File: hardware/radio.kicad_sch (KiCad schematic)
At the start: 61 parts, among them J1 105450-0101, J2 Conn_01x02, J3 Conn_01x02, J4 Conn_01x04, J5 Conn_01x02_Male, Q1 Q_PMOS_DGS, Q2 Q_NMOS_DGS, Q3 Q_NMOS_DGS, Q4 Q_PMOS_DGS, SW1 SW_BOOT, SW2 SW_RST, SW3 SW_1, SW4 Rot_Enc, SW5 SW_2, SW6 SW_3, U1 TP4056, U2 ESP32-WROOM-32, U3 TPS5432, U4 MAX98357

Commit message: routing
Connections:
- net BTN_1: now also U2.28 (IO17)
- net BTN_2: now also U2.27 (IO16)
- net BTN_3: now also U2.26 (IO4)
- net ENC_A: now also U2.5 (SENSOR_VN)
- net ENC_B: now also U2.4 (SENSOR_VP)
- net OLED_RST: now reaches U2.10 (IO25)
- net OLED_RST: now also DISP1.1 (RES)
- net CHRG: now reaches U2.29 (IO5)
- net CHRG: now also U1.7 (~{CHRG})
- net STBY: now reaches U2.30 (IO18)
- net STBY: now also U1.6 (~{STBY})
- net OLED_MOSI: now reaches U2.6 (IO34)
- net OLED_MOSI: now also DISP1.5 (DIN)
- net OLED_CLK: now reaches U2.7 (IO35)
- net OLED_CLK: now also DISP1.4 (CLK)
- net OLED_CS: now reaches U2.8 (IO32)
- net OLED_CS: now also DISP1.3 (CS)
- net OLED_DC: now reaches U2.9 (IO33)
- net OLED_DC: now also DISP1.2 (D/C)
- no-connect marks 6 -> 26
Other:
- note removed: "TODO: * CONNECT DISPLAY AND DAC/AMP TO ESP32 * CONNECT BUTTONS, ROTARY ENCODER"

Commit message: routing
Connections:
- net BTN_1: now also U2.29 (IO5); no longer U2.28 (IO17)
- net BTN_2: now also U2.26 (IO4); no longer U2.27 (IO16)
- net BTN_3: now also U2.27 (IO16); no longer U2.26 (IO4)
- net CHRG: now also U2.30 (IO18); no longer U2.29 (IO5)
- net PWR_CTRL: now also U2.28 (IO17)
- net STBY: now also U2.31 (IO19); no longer U2.30 (IO18)
- no-connect marks 26 -> 25
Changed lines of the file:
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@@
   (no_connect (at 162.56 125.73))
   (no_connect (at 162.56 130.81))
-  (no_connect (at 162.56 123.19))
   (no_connect (at 25.4 93.98))
   (no_connect (at 25.4 83.82))
@@
     (stroke (width 0) (type default) (color 0 0 0 0))
   )
+  (wire (pts (xy 162.56 123.19) (xy 167.64 123.19))
+    (stroke (width 0) (type default) (color 0 0 0 0))
+  )
   (wire (pts (xy 115.57 154.94) (xy 115.57 153.67))
     (stroke (width 0) (type default) (color 0 0 0 0))
@@
     (effects (font (size 1.27 1.27)) (justify left bottom))
   )
-  (global_label "BTN_1" (shape input) (at 167.64 118.11 0) (fields_autoplaced)
-    (effects (font (size 1.27 1.27)) (justify left))
-    (property "Intersheet References" "${INTERSHEET_REFS}" (id 0) (at 175.7983 118.0306 0)
-      (effects (font (size 1.27 1.27)) (justify left) hide)
-    )
-  )
   (global_label "OLED_CLK" (shape input) (at 248.92 95.25 180) (fields_autoplaced)
     (effects (font (size 1.27 1.27)) (justify right))
@@
     )
   )
-  (global_label "BTN_2" (shape input) (at 167.64 115.57 0) (fields_autoplaced)
+  (global_label "BTN_3" (shape input) (at 167.64 115.57 0) (fields_autoplaced)
     (effects (font (size 1.27 1.27)) (justify left))
     (property "Intersheet References" "${INTERSHEET_REFS}" (id 0) (at 175.7983 115.4906 0)
@@
     )
   )
+  (global_label "BTN_1" (shape input) (at 167.64 102.87 0) (fields_autoplaced)
+    (effects (font (size 1.27 1.27)) (justify left))
+    (property "Intersheet References" "${INTERSHEET_REFS}" (id 0) (at 175.7983 102.7906 0)
+      (effects (font (size 1.27 1.27)) (justify left) hide)
+    )
+  )
   (global_label "I2S_SD_MODE" (shape input) (at 199.39 143.51 180) (fields_autoplaced)
     (effects (font (size 1.27 1.27)) (justify right))
@@
     )
   )
-  (global_label "STBY" (shape input) (at 167.64 120.65 0) (fields_autoplaced)
-    (effects (font (size 1.27 1.27)) (justify left))
-    (property "Intersheet References" "${INTERSHEET_REFS}" (id 0) (at 174.5888 120.5706 0)
+  (global_label "PWR_CTRL" (shape input) (at 167.64 118.11 0) (fields_autoplaced)
+    (effects (font (size 1.27 1.27)) (justify left))
+    (property "Intersheet References" "${INTERSHEET_REFS}" (id 0) (at 179.5479 118.0306 0)
       (effects (font (size 1.27 1.27)) (justify left) hide)
     )
@@
     )
   )
+  (global_label "BTN_2" (shape input) (at 167.64 100.33 0) (fields_autoplaced)
+    (effects (font (size 1.27 1.27)) (justify left))
+    (property "Intersheet References" "${INTERSHEET_REFS}" (id 0) (at 175.7983 100.2506 0)
+      (effects (font (size 1.27 1.27)) (justify left) hide)
+    )
+  )
+  (global_label "CHRG" (shape input) (at 167.64 120.65 0) (fields_autoplaced)
+    (effects (font (size 1.27 1.27)) (justify left))
+    (property "Intersheet References" "${INTERSHEET_REFS}" (id 0) (at 175.1936 120.5706 0)
+      (effects (font (size 1.27 1.27)) (justify left) hide)
+    )
+  )
   (global_label "ENC_A" (shape input) (at 129.54 104.14 270) (fields_autoplaced)
     (effects (font (size 1.27 1.27)) (justify right))
@@
     )
   )
-  (global_label "BTN_3" (shape input) (at 167.64 100.33 0) (fields_autoplaced)
-    (effects (font (size 1.27 1.27)) (justify left))
-    (property "Intersheet References" "${INTERSHEET_REFS}" (id 0) (at 175.7983 100.2506 0)
-      (effects (font (size 1.27 1.27)) (justify left) hide)
-    )
-  )
   (global_label "I2S_BCLK" (shape input) (at 167.64 110.49 0) (fields_autoplaced)
     (effects (font (size 1.27 1.27)) (justify left))
@@
     )
   )
-  (global_label "CHRG" (shape input) (at 167.64 102.87 0) (fields_autoplaced)
-    (effects (font (size 1.27 1.27)) (justify left))
-    (property "Intersheet References" "${INTERSHEET_REFS}" (id 0) (at 175.1936 102.7906 0)
-      (effects (font (size 1.27 1.27)) (justify left) hide)
-    )
-  )
   (global_label "ENC_S1" (shape input) (at 107.95 116.84 0) (fields_autoplaced)
     (effects (font (size 1.27 1.27)) (justify left))
@@
       (effects (font (size 1.27 1.27)) (justify left) hide)
     )
+  )
+  (global_label "STBY" (shape input) (at 167.64 123.19 0) (fields_autoplaced)
+    (effects (font (size 1.27 1.27)) (justify left))
+    (property "Intersheet References" "${INTERSHEET_REFS}" (id 0) (at 174.5888 123.1106 0)
+      (effects (font (size 1.27 1.27)) (justify left) hide)
+    )

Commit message: fixed DRC  violations, added silkscreen legend
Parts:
- J1: sklep (none) -> https://kamami.pl/zlacza-usb/1178195-1054500101-zlacze-usb-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
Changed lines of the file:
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@@
       (effects (font (size 1.27 1.27)) (justify left bottom) hide)
+    )
+    (property "sklep" "https://kamami.pl/zlacza-usb/1178195-1054500101-zlacze-usb-typu-c-katowe.html" (id 8) (at 43.18 91.44 0)
+      (effects (font (size 1.27 1.27)) hide)
     )
     (pin "A1")

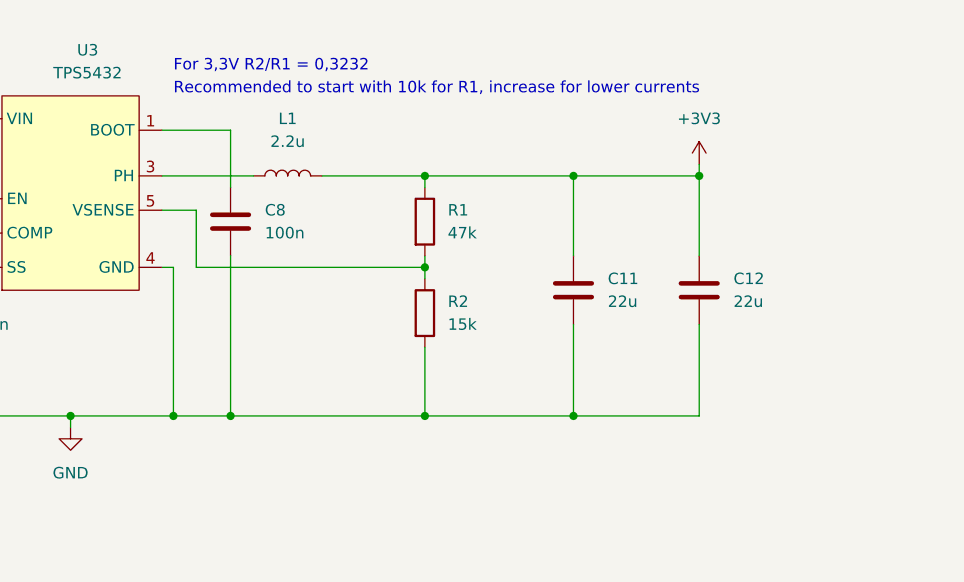
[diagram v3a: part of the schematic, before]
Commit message: Fixed C8 connection from BOOT-GND to BOOT-PH
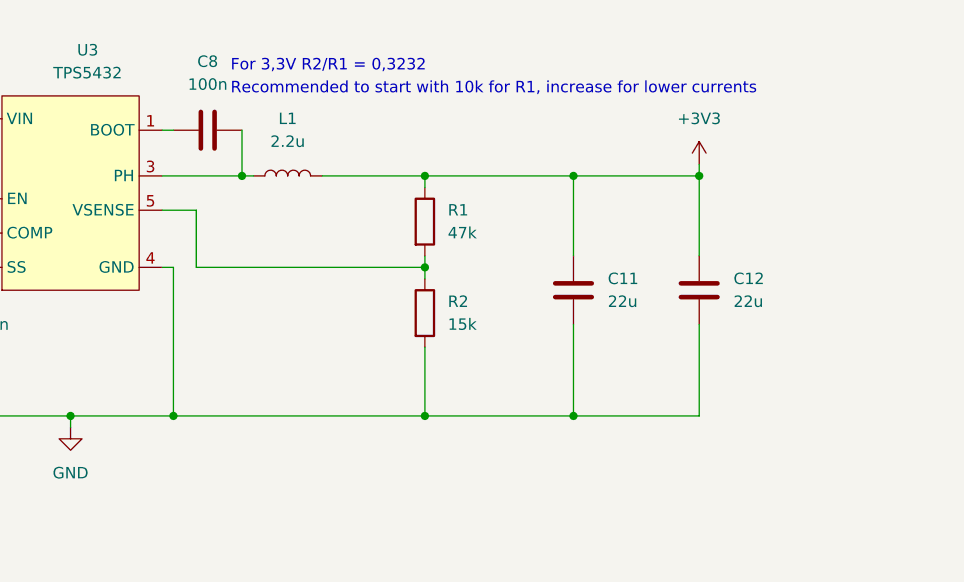
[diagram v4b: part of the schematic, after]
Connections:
- net GND: no longer C8.1
- net at L1.1, U3.3 (PH): now also C8.1
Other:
- moved on the sheet: C8
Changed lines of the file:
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@@
   (junction (at 130.81 22.86) (diameter 0) (color 0 0 0 0)
   )
-  (junction (at 222.25 55.88) (diameter 0) (color 0 0 0 0)
-  )
   (junction (at 85.09 116.84) (diameter 0) (color 0 0 0 0)
+  )
+  (junction (at 223.52 29.21) (diameter 0) (color 0 0 0 0)
   )
   (junction (at 234.95 135.89) (diameter 0) (color 0 0 0 0)
@@
     (stroke (width 0) (type default) (color 0 0 0 0))
   )
+  (wire (pts (xy 214.63 24.13) (xy 215.9 24.13))
+    (stroke (width 0) (type default) (color 0 0 0 0))
+  )
   (wire (pts (xy 19.05 39.37) (xy 19.05 43.18))
     (stroke (width 0) (type default) (color 0 0 0 0))
@@
     (stroke (width 0) (type default) (color 0 0 0 0))
   )
-  (wire (pts (xy 214.63 29.21) (xy 224.79 29.21))
+  (wire (pts (xy 214.63 29.21) (xy 223.52 29.21))
     (stroke (width 0) (type default) (color 0 0 0 0))
   )
@@
     (stroke (width 0) (type default) (color 0 0 0 0))
   )
-  (wire (pts (xy 214.63 24.13) (xy 222.25 24.13))
-    (stroke (width 0) (type default) (color 0 0 0 0))
-  )
   (wire (pts (xy 102.87 119.38) (xy 102.87 116.84))
     (stroke (width 0) (type default) (color 0 0 0 0))
@@
     (stroke (width 0) (type default) (color 0 0 0 0))
   )
+  (wire (pts (xy 223.52 24.13) (xy 223.52 29.21))
+    (stroke (width 0) (type default) (color 0 0 0 0))
+  )
   (wire (pts (xy 62.23 68.58) (xy 43.18 68.58))
     (stroke (width 0) (type default) (color 0 0 0 0))
@@
     (stroke (width 0) (type default) (color 0 0 0 0))
   )
-  (wire (pts (xy 243.84 55.88) (xy 222.25 55.88))
+  (wire (pts (xy 215.9 55.88) (xy 243.84 55.88))
     (stroke (width 0) (type default) (color 0 0 0 0))
   )
@@
     (stroke (width 0) (type default) (color 0 0 0 0))
   )
-  (wire (pts (xy 222.25 55.88) (xy 215.9 55.88))
-    (stroke (width 0) (type default) (color 0 0 0 0))
-  )
   (wire (pts (xy 85.09 115.57) (xy 85.09 116.84))
     (stroke (width 0) (type default) (color 0 0 0 0))
@@
     (stroke (width 0) (type default) (color 0 0 0 0))
   )
+  (wire (pts (xy 223.52 29.21) (xy 224.79 29.21))
+    (stroke (width 0) (type default) (color 0 0 0 0))
+  )
   (wire (pts (xy 85.09 129.54) (xy 95.25 129.54))
     (stroke (width 0) (type default) (color 0 0 0 0))
@@
     (stroke (width 0) (type default) (color 0 0 0 0))
   )
-  (wire (pts (xy 222.25 38.1) (xy 222.25 55.88))
-    (stroke (width 0) (type default) (color 0 0 0 0))
-  )
   (wire (pts (xy 187.96 99.06) (xy 187.96 100.33))
     (stroke (width 0) (type default) (color 0 0 0 0))
@@
   )
   (wire (pts (xy 204.47 55.88) (xy 215.9 55.88))
-    (stroke (width 0) (type default) (color 0 0 0 0))
-  )
-  (wire (pts (xy 222.25 24.13) (xy 222.25 30.48))
     (stroke (width 0) (type default) (color 0 0 0 0))
   )
@@
   )
   (text "Recommended to start with 10k for R1, increase for lower currents"
-    (at 215.9 20.32 0)
+    (at 222.25 20.32 0)
     (effects (font (size 1.27 1.27)) (justify left bottom))
   )
@@
     (effects (font (size 1.27 1.27)) (justify left bottom))
   )
-  (text "For 3,3V R2/R1 = 0,3232" (at 215.9 17.78 0)
+  (text "For 3,3V R2/R1 = 0,3232" (at 222.25 17.78 0)
     (effects (font (size 1.27 1.27)) (justify left bottom))
   )
@@
     (pin "2")
   )
-  (symbol (lib_id "Device:C") (at 222.25 34.29 180) (unit 1)
-    (in_bom yes) (on_board yes) (fields_autoplaced)
-    (property "Reference" "C8" (id 0) (at 226.06 33.0199 0)
-      (effects (font (size 1.27 1.27)) (justify right))
-    )
-    (property "Value" "100n" (id 1) (at 226.06 35.5599 0)
-      (effects (font (size 1.27 1.27)) (justify right))
-    )
-    (property "Footprint" "Capacitor_SMD:C_0603_1608Metric" (id 2) (at 221.2848 30.48 0)
-      (effects (font (size 1.27 1.27)) hide)
-    )
-    (property "Datasheet" "~" (id 3) (at 222.25 34.29 0)
-      (effects (font (size 1.27 1.27)) hide)
-    )
-    (property "Voltage rating" ">10V" (id 4) (at 222.25 34.29 0)
-      (effects (font (size 1.27 1.27)) hide)
-    )
-    (property "Dielectric" "X5R or X7R" (id 5) (at 222.25 34.29 0)
-      (effects (font (size 1.27 1.27)) hide)
-    )
+  (symbol (lib_id "Device:C") (at 219.71 24.13 270) (unit 1)
+    (in_bom yes) (on_board yes) (fields_autoplaced)
+    (property "Reference" "C8" (id 0) (at 219.71 16.51 90))
+    (property "Value" "100n" (id 1) (at 219.71 19.05 90))
+    (property "Footprint" "Capacitor_SMD:C_0603_1608Metric" (id 2) (at 215.9 25.0952 0)
+      (effects (font (size 1.27 1.27)) hide)
+    )
+    (property "Datasheet" "~" (id 3) (at 219.71 24.13 0)
+      (effects (font (size 1.27 1.27)) hide)
+    )
+    (property "Voltage rating" ">10V" (id 4) (at 219.71 24.13 0)
+      (effects (font (size 1.27 1.27)) hide)
+    )
+    (property "Dielectric" "X5R or X7R" (id 5) (at 219.71 24.13 0)
+      (effects (font (size 1.27 1.27)) hide)
+    )

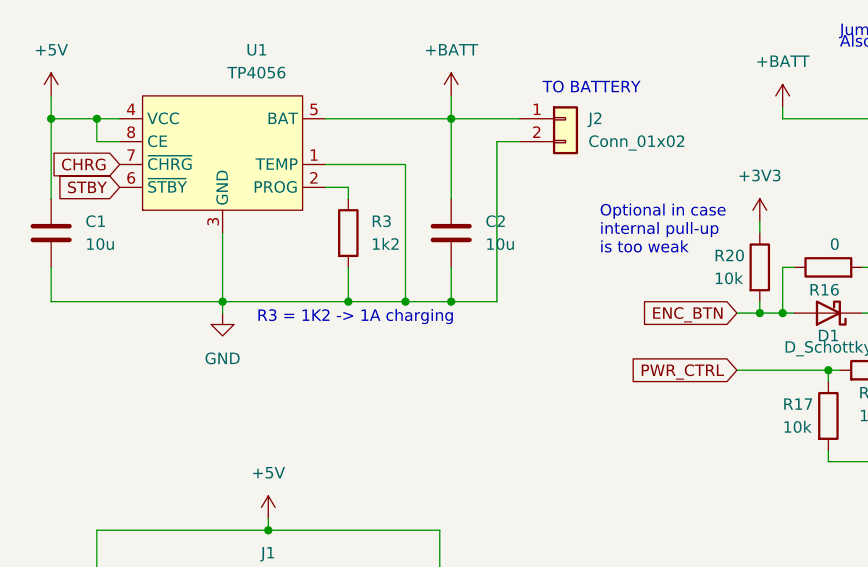
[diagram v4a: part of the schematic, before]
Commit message: Added 0.4 ohm 0.5 W resistor to TP4056 to help with power dissipation
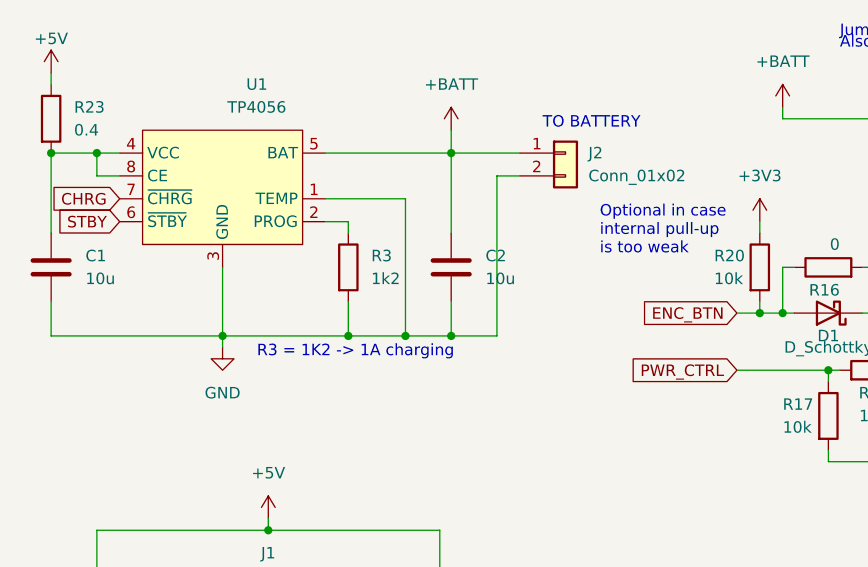
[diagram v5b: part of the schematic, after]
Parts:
- added R23: 0.4, Resistor_SMD:R_1210_3225Metric, symbol Device:R
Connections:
- net +5V: now also R23.1; no longer C1.1, U1.4 (VCC), U1.8 (CE)
- new net: C1.1, R23.2, U1.4 (VCC), U1.8 (CE)
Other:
- moved on the sheet: C1, C2, J2, R3, U1

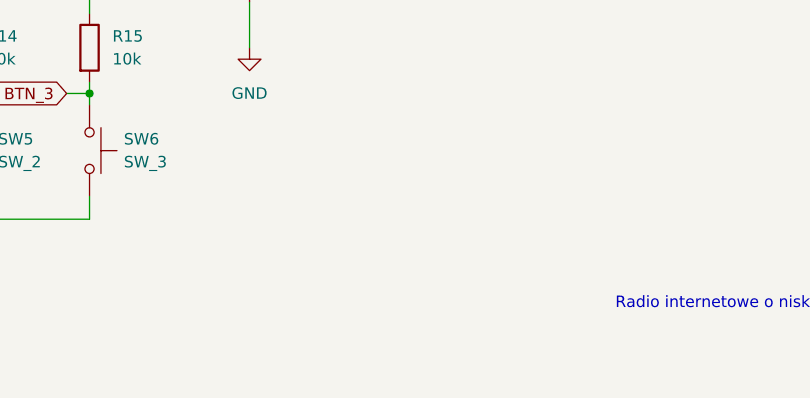
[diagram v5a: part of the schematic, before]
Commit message: added test points; corrected C5 silkscreen again
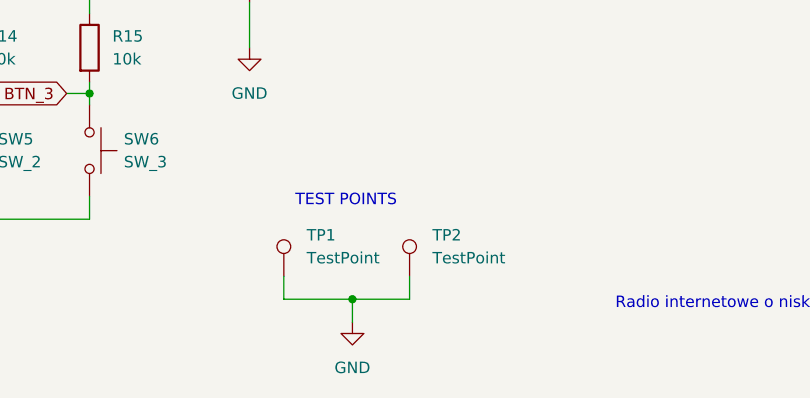
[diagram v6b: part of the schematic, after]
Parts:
- added TP1, TP2: TestPoint, symbol Connector:TestPoint
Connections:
- net GND: now also TP1.1, TP2.1
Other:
- note added: "TEST POINTS"
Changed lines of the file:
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@@
   (junction (at 161.29 55.88) (diameter 0) (color 0 0 0 0)
   )
+  (junction (at 158.75 189.23) (diameter 0) (color 0 0 0 0)
+  )
   (junction (at 124.46 60.96) (diameter 0) (color 0 0 0 0)
   )
@@
     (stroke (width 0) (type default) (color 0 0 0 0))
   )
+  (wire (pts (xy 151.13 189.23) (xy 158.75 189.23))
+    (stroke (width 0) (type default) (color 0 0 0 0))
+  )
   (wire (pts (xy 162.56 140.97) (xy 167.64 140.97))
     (stroke (width 0) (type default) (color 0 0 0 0))
@@
     (stroke (width 0) (type default) (color 0 0 0 0))
   )
+  (wire (pts (xy 151.13 186.69) (xy 151.13 189.23))
+    (stroke (width 0) (type default) (color 0 0 0 0))
+  )
   (wire (pts (xy 215.9 134.62) (xy 215.9 135.89))
     (stroke (width 0) (type default) (color 0 0 0 0))
@@
     (stroke (width 0) (type default) (color 0 0 0 0))
   )
+  (wire (pts (xy 158.75 189.23) (xy 165.1 189.23))
+    (stroke (width 0) (type default) (color 0 0 0 0))
+  )
   (wire (pts (xy 229.87 130.81) (xy 234.95 130.81))
     (stroke (width 0) (type default) (color 0 0 0 0))
@@
     (stroke (width 0) (type default) (color 0 0 0 0))
   )
+  (wire (pts (xy 165.1 186.69) (xy 165.1 189.23))
+    (stroke (width 0) (type default) (color 0 0 0 0))
+  )
   (wire (pts (xy 243.84 29.21) (xy 260.35 29.21))
     (stroke (width 0) (type default) (color 0 0 0 0))
@@
     (stroke (width 0) (type default) (color 0 0 0 0))
   )
+  (wire (pts (xy 158.75 189.23) (xy 158.75 191.77))
+    (stroke (width 0) (type default) (color 0 0 0 0))
+  )
   (wire (pts (xy 149.86 22.86) (xy 161.29 22.86))
     (stroke (width 0) (type default) (color 0 0 0 0))
@@
     (effects (font (size 1.27 1.27)) (justify left bottom))
   )
+  (text "TEST POINTS" (at 152.4 179.07 0)
+    (effects (font (size 1.27 1.27)) (justify left bottom))
+  )
   (text "Also for easy current measurements" (at 106.68 15.24 0)
     (effects (font (size 1.27 1.27)) (justify left bottom))
@@
     (pin "1")
   )
+  (symbol (lib_id "Connector:TestPoint") (at 151.13 186.69 0) (unit 1)
+    (in_bom yes) (on_board yes) (fields_autoplaced)
+    (property "Reference" "TP1" (id 0) (at 153.67 182.1179 0)
+      (effects (font (size 1.27 1.27)) (justify left))
+    )
+    (property "Value" "TestPoint" (id 1) (at 153.67 184.6579 0)
+      (effects (font (size 1.27 1.27)) (justify left))
+    )
+    (property "Footprint" "" (id 2) (at 156.21 186.69 0)
+      (effects (font (size 1.27 1.27)) hide)
+    )
+    (property "Datasheet" "~" (id 3) (at 156.21 186.69 0)
+      (effects (font (size 1.27 1.27)) hide)
+    )
+    (pin "1")
+  )
   (symbol (lib_id "Device:R") (at 100.33 161.29 0) (unit 1)
     (in_bom yes) (on_board yes) (fields_autoplaced)
@@
     (pin "2")
   )
+  (symbol (lib_id "Connector:TestPoint") (at 165.1 186.69 0) (unit 1)
+    (in_bom yes) (on_board yes) (fields_autoplaced)
+    (property "Reference" "TP2" (id 0) (at 167.64 182.1179 0)
+      (effects (font (size 1.27 1.27)) (justify left))
+    )
+    (property "Value" "TestPoint" (id 1) (at 167.64 184.6579 0)
+      (effects (font (size 1.27 1.27)) (justify left))
+    )
+    (property "Footprint" "" (id 2) (at 170.18 186.69 0)
+      (effects (font (size 1.27 1.27)) hide)
+    )
+    (property "Datasheet" "~" (id 3) (at 170.18 186.69 0)
+      (effects (font (size 1.27 1.27)) hide)
+    )
+    (pin "1")
+  )
   (symbol (lib_id "power:+5V") (at 43.18 67.31 0) (unit 1)
     (in_bom yes) (on_board yes) (fields_autoplaced)
@@
     (pin "2")
   )
+  (symbol (lib_id "power:GND") (at 158.75 191.77 0) (unit 1)
+    (in_bom yes) (on_board yes) (fields_autoplaced)
+    (property "Reference" "#PWR?" (id 0) (at 158.75 198.12 0)
+      (effects (font (size 1.27 1.27)) hide)
+    )
+    (property "Value" "GND" (id 1) (at 158.75 196.85 0))
+    (property "Footprint" "" (id 2) (at 158.75 191.77 0)
+      (effects (font (size 1.27 1.27)) hide)
+    )
+    (property "Datasheet" "" (id 3) (at 158.75 191.77 0)
+      (effects (font (size 1.27 1.27)) hide)
+    )
+    (pin "1")
+  )
   (symbol (lib_id "power:+3V3") (at 274.32 27.94 0) (unit 1)
     (in_bom yes) (on_board yes) (fields_autoplaced)
@@
       (reference "#PWR0124") (unit 1) (value "+3V3") (footprint "")
     )
+    (path "/f73179c7-64e4-4f62-9c58-7c3400f3435c"
+      (reference "#PWR?") (unit 1) (value "GND") (footprint "")
+    )
     (path "/31276b67-1ce3-42d3-a55d-ef9419463436"
       (reference "C1") (unit 1) (value "10u") (footprint "Capacitor_SMD:C_1206_3216Metric")
@@
       (reference "SW6") (unit 1) (value "SW_3") (footprint "Button_Switch_SMD:SW_Push_1P1T_NO_6x6mm_H9.5mm")
     )
+    (path "/25c71baa-00a8-4ec2-be04-656a7bf9cecb"
+      (reference "TP1") (unit 1) (value "TestPoint") (footprint "")
+    )
+    (path "/e9301eb0-4603-469f-9fe6-01969d48b33c"
+      (reference "TP2") (unit 1) (value "TestPoint") (footprint "")
+    )
     (path "/a274958a-ae53-4989-b48b-9f41b3964f32"
